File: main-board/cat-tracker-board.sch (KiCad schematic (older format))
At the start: 29 parts, among them J1 Conn_01x10, J3 USB_B_Micro, Q1 SI3443DDV-T1-GE3, SW1 PCM12SMTR, U1 ATSAMD21E18A-M, U3 L80-R, U4 RFM95W-915S2, U5 MCP73831-2ACI/MC, U6 MCP1700T-3602E/TT

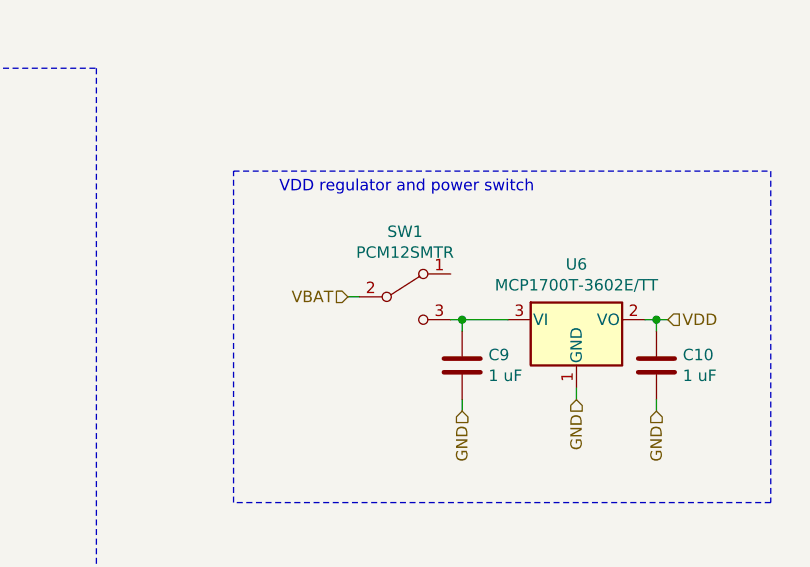
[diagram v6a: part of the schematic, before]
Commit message: Change switch connection to improve layout.
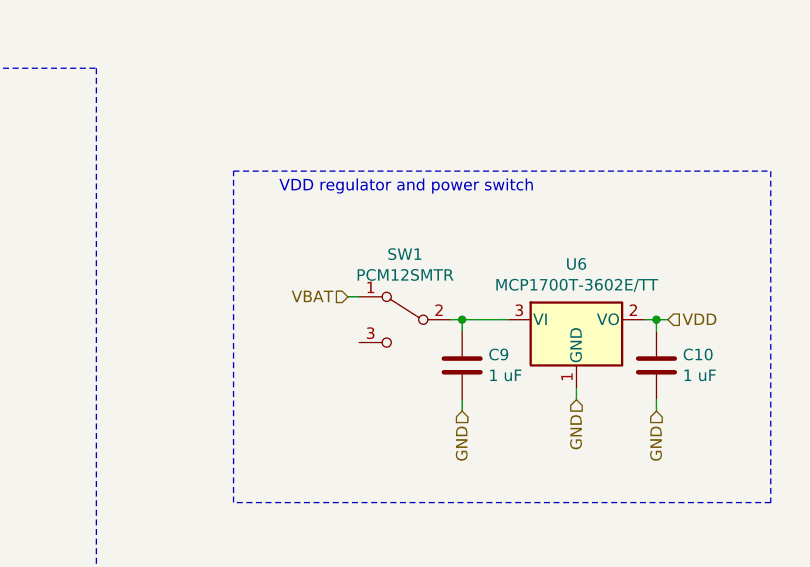
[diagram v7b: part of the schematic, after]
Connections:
- net VBAT: now also SW1.1 (A); no longer SW1.2 (B)
- net at C9.1, U6.3 (VI): now also SW1.2 (B); no longer SW1.3 (C)
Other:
- moved on the sheet: SW1
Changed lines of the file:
@@
 L Switch:SW_SPDT SW1
 U 1 1 60C01EB4
-P 10550 7950
-F 0 "SW1" H 10550 8235 50  0000 C CNN
-F 1 "PCM12SMTR" H 10550 8144 50  0000 C CNN
-F 2 "Button_Switch_SMD:SW_SPDT_PCM12" H 10550 7950 50  0001 C CNN
-F 3 "~" H 10550 7950 50  0001 C CNN
-F 4 "C&K" H 10550 7950 50  0001 C CNN "mfg1"
-F 5 "PCM12SMTR" H 10550 7950 50  0001 C CNN "mfg1pn"
-	1    10550 7950
-	1    0    0    -1
+P 10550 8050
+F 0 "SW1" H 10550 8335 50  0000 C CNN
+F 1 "PCM12SMTR" H 10550 8244 50  0000 C CNN
+F 2 "Button_Switch_SMD:SW_SPDT_PCM12" H 10550 8050 50  0001 C CNN
+F 3 "~" H 10550 8050 50  0001 C CNN
+F 4 "C&K" H 10550 8050 50  0001 C CNN "mfg1"
+F 5 "PCM12SMTR" H 10550 8050 50  0001 C CNN "mfg1pn"
+	1    10550 8050
+	-1   0    0    -1
 $EndComp
 Text HLabel 11700 8050 2    50   Input ~ 0

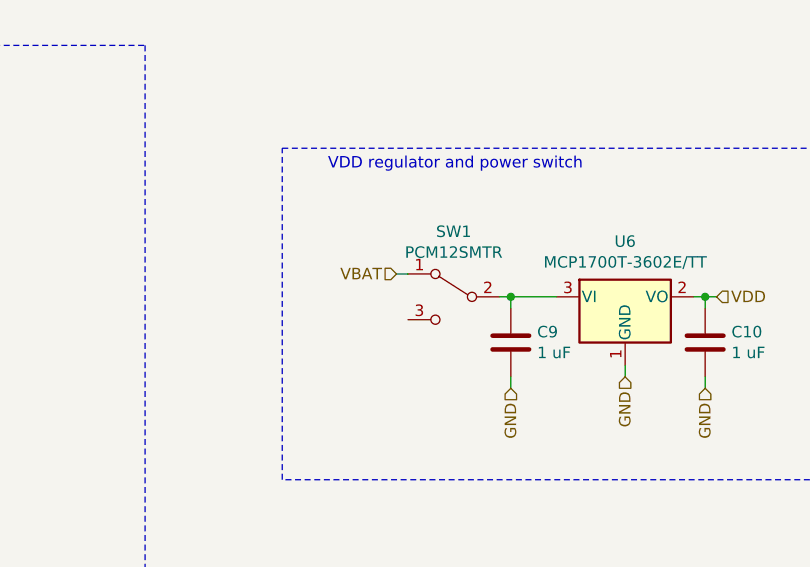
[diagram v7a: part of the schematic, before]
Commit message: Correct footprint assignment for U5 and work on layout.
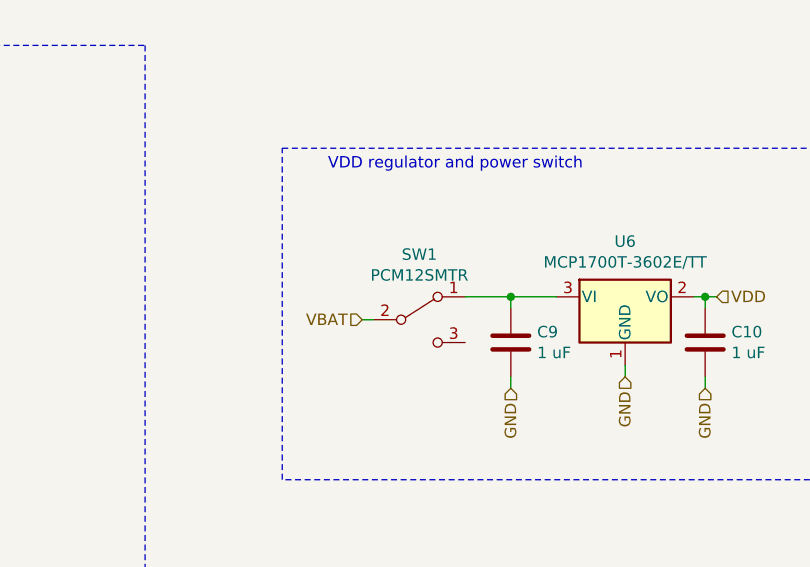
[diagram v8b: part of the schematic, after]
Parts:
- U5: footprint Package_DFN_QFN:DFN-8_2x2mm_P0.5mm -> Package_DFN_QFN:DFN-8-1EP_3x2mm_P0.5mm_EP1.75x1.45mm
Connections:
- net VBAT: now also SW1.2 (B); no longer SW1.1 (A)
- net at C9.1, U6.3 (VI): now also SW1.1 (A); no longer SW1.2 (B)
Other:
- moved on the sheet: SW1
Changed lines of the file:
@@
 	1    0    0    -1
 $EndComp
-Text HLabel 10300 7950 0    50   Input ~ 0
+Text HLabel 10150 8150 0    50   Input ~ 0
 VBAT
 Wire Wire Line
-	10300 7950 10350 7950
+	10150 8150 10200 8150
 $Comp
 L Switch:SW_SPDT SW1
 U 1 1 60C01EB4
-P 10550 8050
-F 0 "SW1" H 10550 8335 50  0000 C CNN
-F 1 "PCM12SMTR" H 10550 8244 50  0000 C CNN
-F 2 "Button_Switch_SMD:SW_SPDT_PCM12" H 10550 8050 50  0001 C CNN
-F 3 "~" H 10550 8050 50  0001 C CNN
-F 4 "C&K" H 10550 8050 50  0001 C CNN "mfg1"
-F 5 "PCM12SMTR" H 10550 8050 50  0001 C CNN "mfg1pn"
-	1    10550 8050
-	-1   0    0    -1
+P 10400 8150
+F 0 "SW1" H 10400 8435 50  0000 C CNN
+F 1 "PCM12SMTR" H 10400 8344 50  0000 C CNN
+F 2 "Button_Switch_SMD:SW_SPDT_PCM12" H 10400 8150 50  0001 C CNN
+F 3 "~" H 10400 8150 50  0001 C CNN
+F 4 "C&K" H 10400 8150 50  0001 C CNN "mfg1"
+F 5 "PCM12SMTR" H 10400 8150 50  0001 C CNN "mfg1pn"
+	1    10400 8150
+	1    0    0    -1
 $EndComp
 Text HLabel 11700 8050 2    50   Input ~ 0
@@
 F 0 "U5" H 7850 5415 50  0000 C CNN
 F 1 "MCP73831-2ACI/MC" H 7850 5324 50  0000 C CNN
-F 2 "Package_DFN_QFN:DFN-8_2x2mm_P0.5mm" H 7750 4900 50  0001 C CNN
+F 2 "Package_DFN_QFN:DFN-8-1EP_3x2mm_P0.5mm_EP1.75x1.45mm" H 7750 4900 50  0001 C CNN
 F 3 "" H 7750 4900 50  0001 C CNN
 F 4 "Microchip" H 7850 5000 50  0001 C CNN "mfg1"
@@
 $EndComp
 Wire Wire Line
-	10750 8050 10800 8050
-Wire Wire Line
 	11300 8350 11300 8400
 Text HLabel 11300 8400 3    50   Input ~ 0
@@
 Text HLabel 1800 7200 0    50   Input ~ 0
 USBD+
+Wire Wire Line
+	10600 8050 10800 8050
 $EndSCHEMATC
